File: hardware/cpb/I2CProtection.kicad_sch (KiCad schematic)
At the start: 16 parts, among them Q12 MBT2222ADW1T1, Q13 MBT2222ADW1T1, Q14 BSS138PS,115, Q15 BSS138PS,115

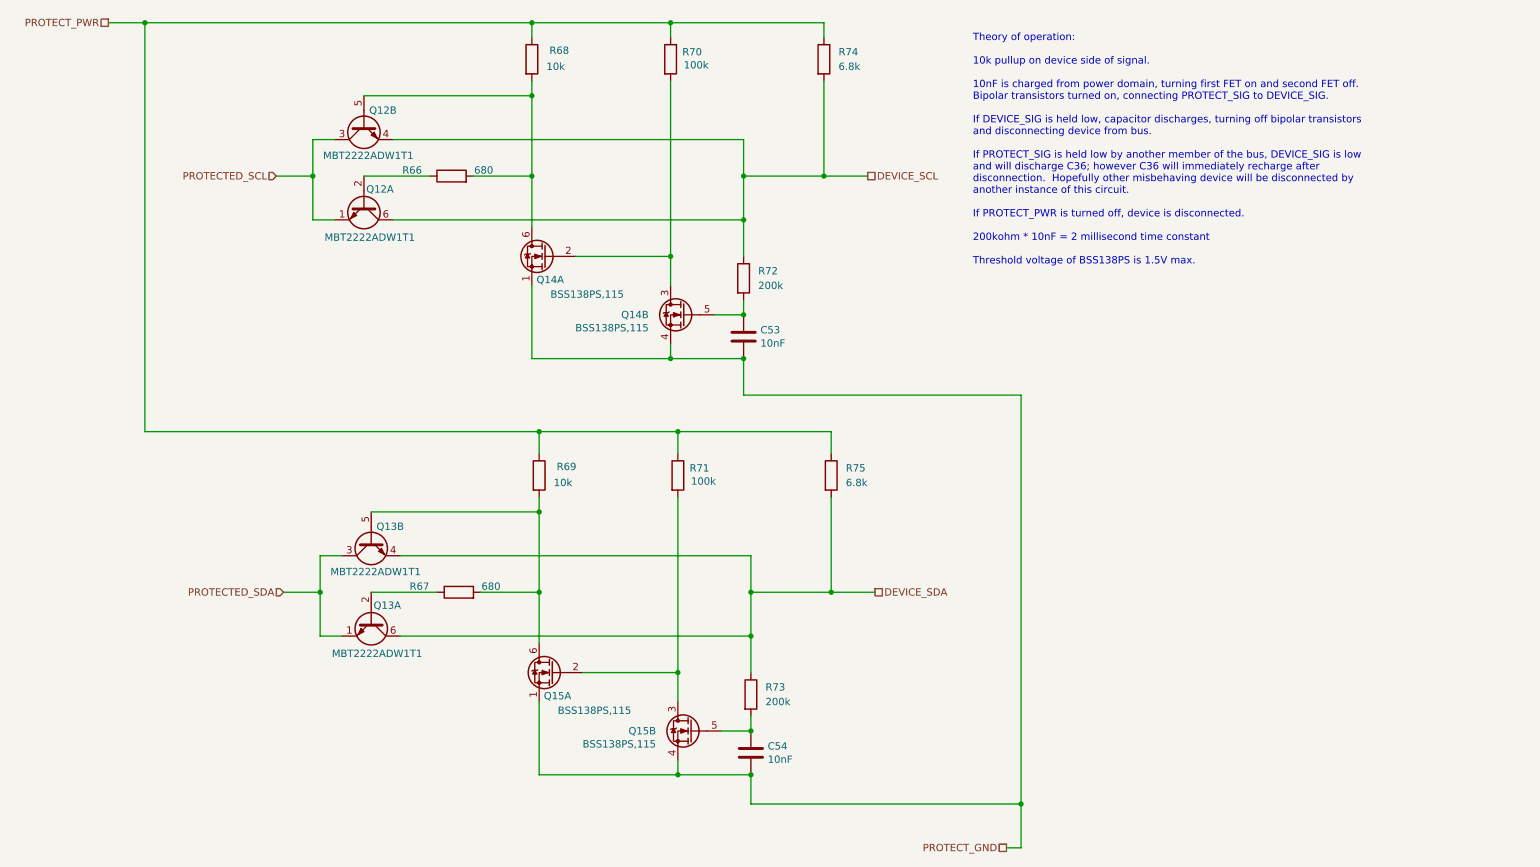
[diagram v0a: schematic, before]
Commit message: hardware/cpb: Transistors on right sorted and bypass capacitors added Moved the transistors into groups then placed next to connectors and placed bypass capacitors near power pins.
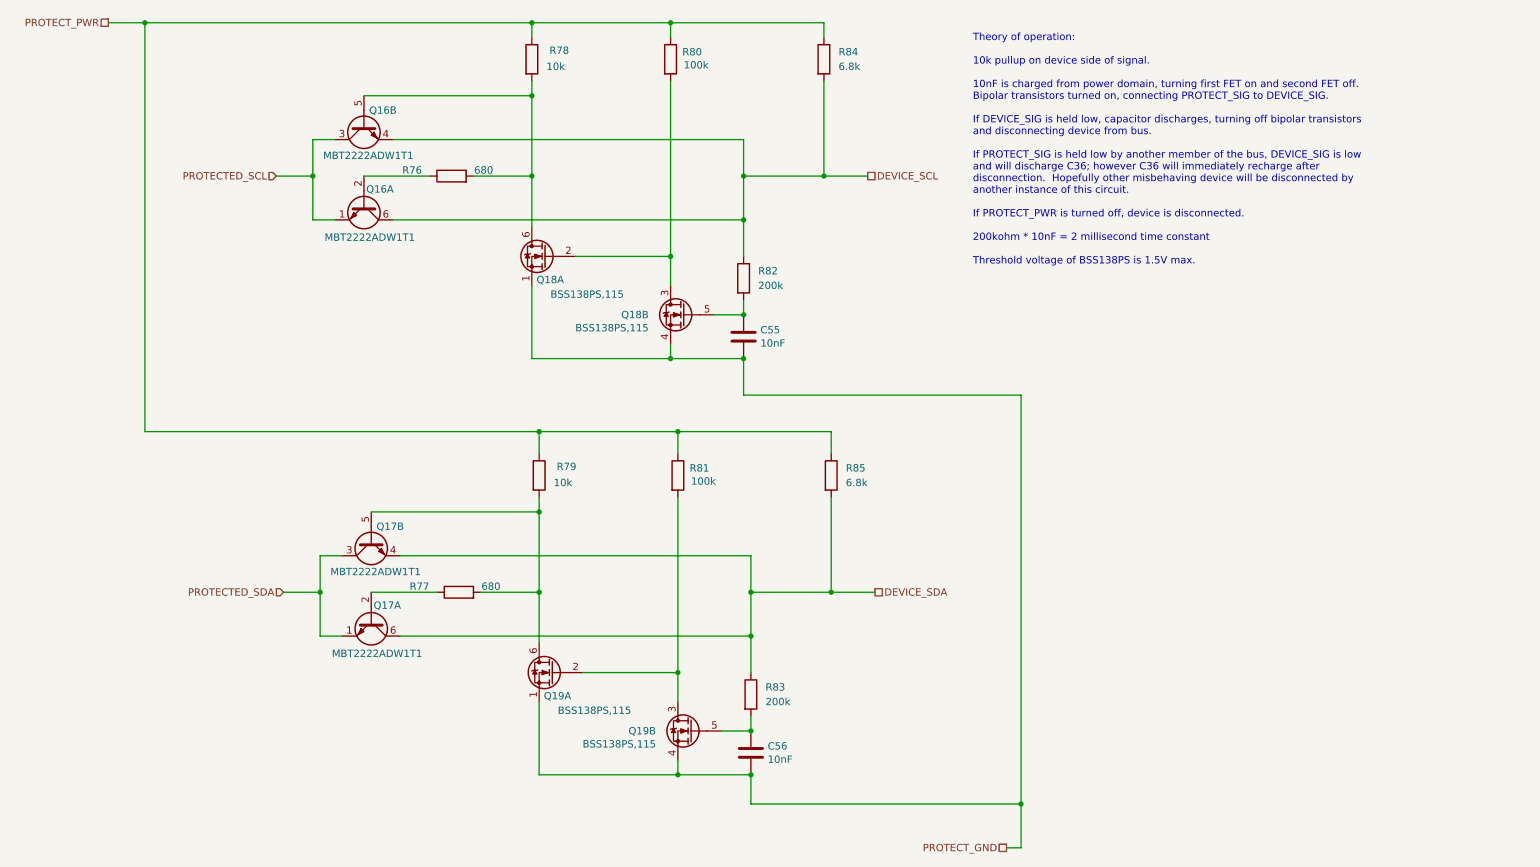
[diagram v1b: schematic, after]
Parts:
- renumbered C53 to C55, C54 to C56, Q12 to Q16, Q13 to Q17, Q14 to Q18, Q15 to Q19, R66 to R76, R67 to R77, R68 to R78, R69 to R79, R70 to R80, R71 to R81, R72 to R82, R73 to R83, R74 to R84, R75 to R85

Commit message: cpb: Bill of materials updates
One layout change will result: some 1206 resistors became 2012.
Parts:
- C55, C56: LCSC (none) -> C100042
- R76, R77: LCSC (none) -> C3996690
- R78, R79: LCSC (none) -> C844918
- R80, R81: LCSC (none) -> C189597
- R82, R83: LCSC (none) -> C118142
- R84, R85: LCSC (none) -> C844805
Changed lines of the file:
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@@
+			)
+		)
+		(property "LCSC" "C844805"
+			(at 161.29 101.6 0)
+			(effects
+				(font
+					(size 1.27 1.27)
+				)
+				(hide yes)
 			)
 		)
@@
 			)
 		)
+		(property "LCSC" "C844918"
+			(at 109.22 29.21 0)
+			(effects
+				(font
+					(size 1.27 1.27)
+				)
+				(hide yes)
+			)
+		)
 		(pin "1"
 		)
@@
 			)
 		)
-		(property "LCSC" ""
+		(property "LCSC" "C100042"
 			(at 147.32 149.86 0)
 			(effects
@@
 		)
 		(property "Description" "Resistor"
+			(at 133.35 29.21 0)
+			(effects
+				(font
+					(size 1.27 1.27)
+				)
+				(hide yes)
+			)
+		)
+		(property "LCSC" "C189597"
 			(at 133.35 29.21 0)
 			(effects
@@
 			)
 		)
+		(property "LCSC" "C118142"
+			(at 146.05 67.31 0)
+			(effects
+				(font
+					(size 1.27 1.27)
+				)
+				(hide yes)
+			)
+		)
 		(pin "1"
 		)
@@
 			)
 		)
+		(property "LCSC" "C3996690"
+			(at 96.52 121.92 0)
+			(effects
+				(font
+					(size 1.27 1.27)
+				)
+				(hide yes)
+			)
+		)
 		(pin "1"
 		)
@@
 		)
 		(property "Description" "Resistor"
+			(at 134.62 101.6 0)
+			(effects
+				(font
+					(size 1.27 1.27)
+				)
+				(hide yes)
+			)
+		)
+		(property "LCSC" "C189597"
 			(at 134.62 101.6 0)
 			(effects
@@
 			)
 		)
+		(property "LCSC" "C118142"
+			(at 147.32 139.7 0)
+			(effects
+				(font
+					(size 1.27 1.27)
+				)
+				(hide yes)
+			)
+		)
 		(pin "1"
 		)
@@
 			)
 		)
+		(property "LCSC" "C3996690"
+			(at 95.25 49.53 0)
+			(effects
+				(font
+					(size 1.27 1.27)
+				)
+				(hide yes)
+			)
+		)
 		(pin "1"
 		)
@@
 			)
 		)
-		(property "LCSC" ""
+		(property "LCSC" "C100042"
 			(at 146.05 77.47 0)
 			(effects
@@
 			)
 		)
+		(property "LCSC" "C844918"
+			(at 110.49 101.6 0)
+			(effects
+				(font
+					(size 1.27 1.27)
+				)
+				(hide yes)
+			)
+		)
 		(pin "1"
 		)
@@
 			(at 160.02 29.21 0)
 			(effects
+				(font
+					(size 1.27 1.27)
+				)
+				(hide yes)
+			)
+		)
+		(property "LCSC" "C844805"
+			(at 160.02 29.21 0)
+			(effects

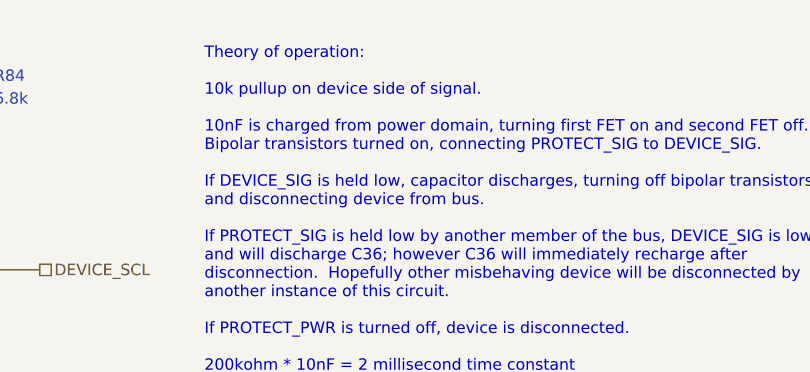
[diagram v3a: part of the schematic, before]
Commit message: cpb: add pours to top and bottom, straighten things
Getting very close, now.
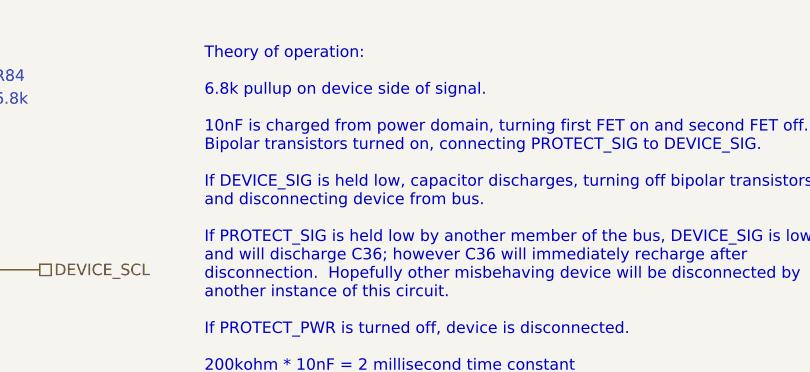
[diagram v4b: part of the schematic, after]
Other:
- note added: "Theory of operation: 6.8k pullup on device side of signal. 10nF is charged from power domain, turning first FET on and second FET off. Bipolar transistors turned on, connecting PROTECT_SIG to DEVICE_SIG. If DEVICE_SIG is held low, capacitor discharges, turning off bipolar transistors and disconnecting device from bus. If PROTECT_SIG is held low by another member of the bus, DEVICE_SIG is low and 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"
- note removed: "Theory of operation: 10k pullup on device side of signal. 10nF is charged from power domain, turning first FET on and second FET off. Bipolar transistors turned on, connecting PROTECT_SIG to DEVICE_SIG. If DEVICE_SIG is held low, capacitor discharges, turning off bipolar transistors and disconnecting device from bus. If PROTECT_SIG is held low by another member of the bus, DEVICE_SIG is low and w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"
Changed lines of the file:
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@@
 		)
 	)
-	(text "Theory of operation:\n\n10k pullup on device side of signal.\n\n10nF is charged from power domain, turning first FET on and second FET off.\nBipolar transistors turned on, connecting PROTECT_SIG to DEVICE_SIG.\n\nIf DEVICE_SIG is held low, capacitor discharges, turning off bipolar transistors\nand disconnecting device from bus.\n\nIf PROTECT_SIG is held low by another member of the bus, DEVICE_SIG is low\nand will discharge C36; however C36 will immediately recharge after\ndisconnection.  Hopefully other misbehaving device will be disconnected by\nanother instance of this circuit.\n\nIf PROTECT_PWR is turned off, device is disconnected.\n\n200kohm * 10nF = 2 millisecond time constant\n\nThreshold voltage of BSS138PS is 1.5V max."
+	(text "Theory of operation:\n\n6.8k pullup on device side of signal.\n\n10nF is charged from power domain, turning first FET on and second FET off.\nBipolar transistors turned on, connecting PROTECT_SIG to DEVICE_SIG.\n\nIf DEVICE_SIG is held low, capacitor discharges, turning off bipolar transistors\nand disconnecting device from bus.\n\nIf PROTECT_SIG is held low by another member of the bus, DEVICE_SIG is low\nand will discharge C36; however C36 will immediately recharge after\ndisconnection.  Hopefully other misbehaving device will be disconnected by\nanother instance of this circuit.\n\nIf PROTECT_PWR is turned off, device is disconnected.\n\n200kohm * 10nF = 2 millisecond time constant\n\nThreshold voltage of BSS138PS is 1.5V max."
 		(exclude_from_sim no)
 		(at 185.928 44.958 0)

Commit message: cpb: update part numbers and attributes
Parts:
- R76, R77: LCSC C3996690 -> C23228
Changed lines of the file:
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@@
 			)
 		)
-		(property "LCSC" "C3996690"
+		(property "LCSC" "C23228"
 			(at 96.52 121.92 0)
 			(effects
@@
 			)
 		)
-		(property "LCSC" "C3996690"
+		(property "LCSC" "C23228"
 			(at 95.25 49.53 0)
 			(effects

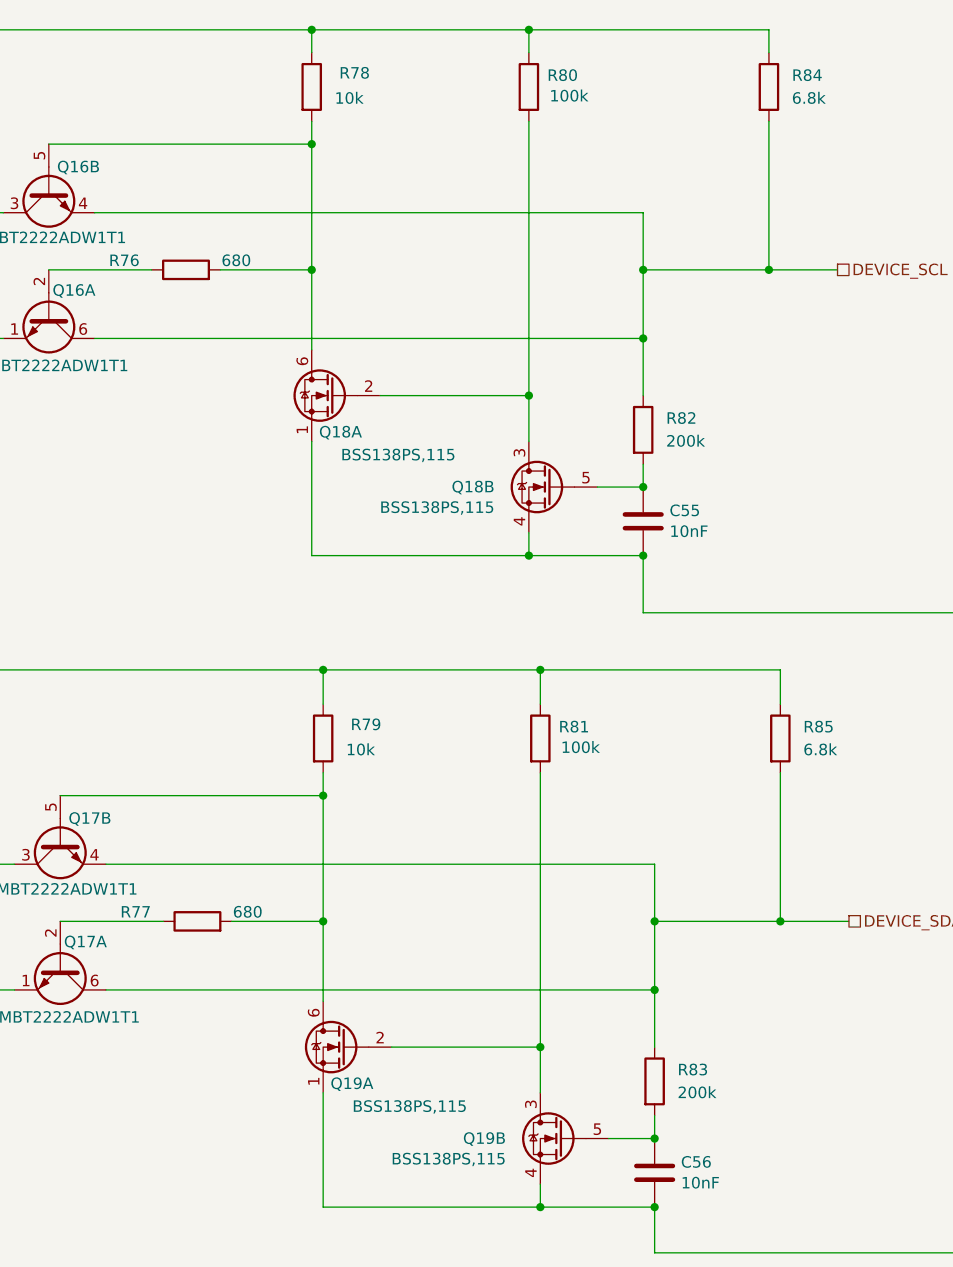
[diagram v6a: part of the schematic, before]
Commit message: hardware/cpb: changed from european to american symbols.
RN parts still are european for now. Changed via TextEdit replace all tool. Device:R --> Device:R_US
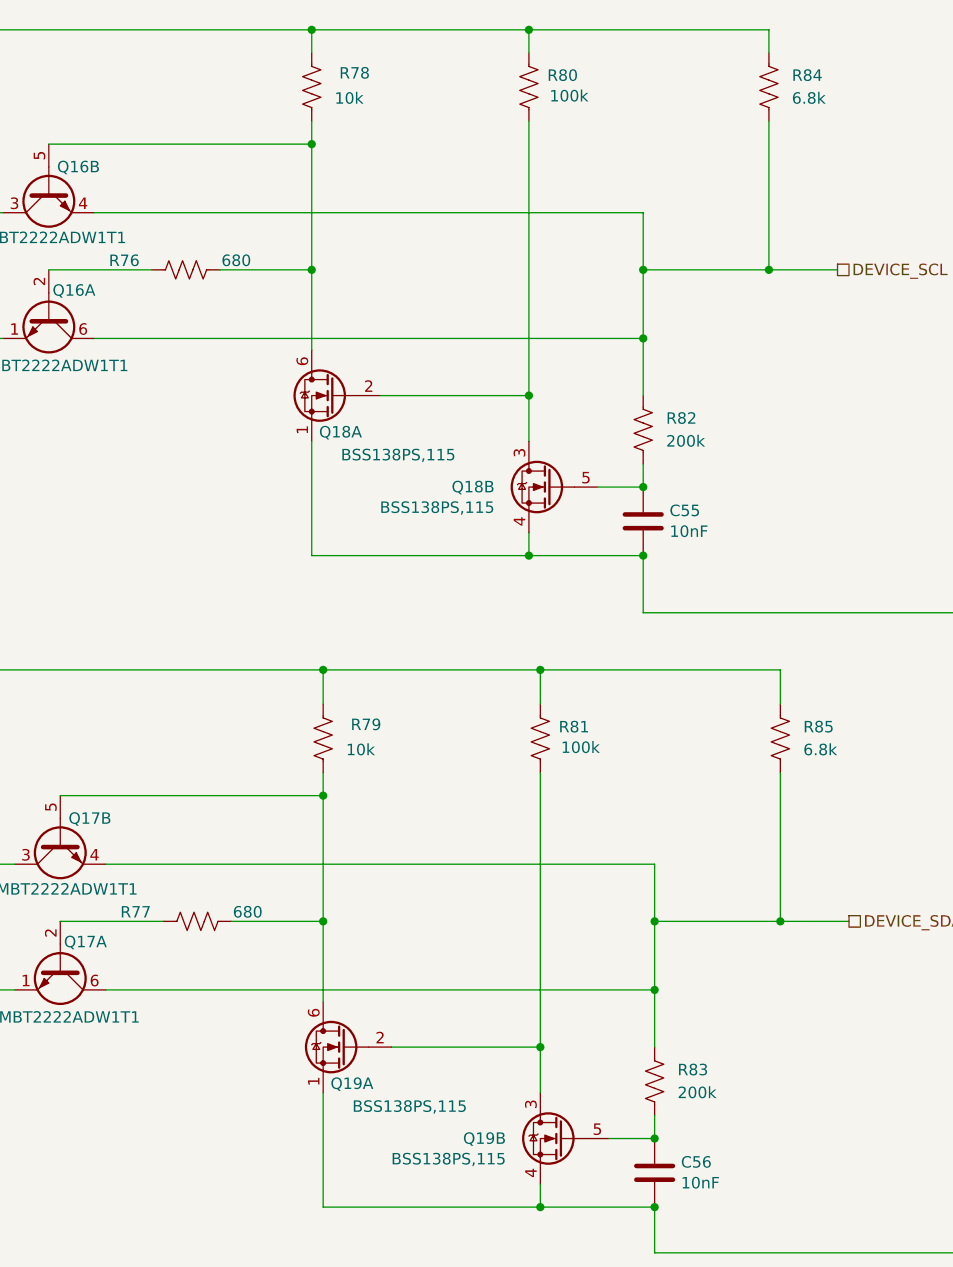
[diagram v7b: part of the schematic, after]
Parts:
- R76, R77, R78, R79, R80, R81, R82, R83, R84, R85: symbol Device:R -> Device:R_US
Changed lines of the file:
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@@
 	)
 	(symbol
-		(lib_id "Device:R")
+		(lib_id "Device:R_US")
 		(at 161.29 101.6 0)
 		(unit 1)
@@
 	)
 	(symbol
-		(lib_id "Device:R")
+		(lib_id "Device:R_US")
 		(at 109.22 29.21 0)
 		(unit 1)
@@
 	)
 	(symbol
-		(lib_id "Device:R")
+		(lib_id "Device:R_US")
 		(at 133.35 29.21 0)
 		(unit 1)
@@
 	)
 	(symbol
-		(lib_id "Device:R")
+		(lib_id "Device:R_US")
 		(at 146.05 67.31 0)
 		(unit 1)
@@
 	)
 	(symbol
-		(lib_id "Device:R")
+		(lib_id "Device:R_US")
 		(at 96.52 121.92 90)
 		(unit 1)
@@
 	)
 	(symbol
-		(lib_id "Device:R")
+		(lib_id "Device:R_US")
 		(at 134.62 101.6 0)
 		(unit 1)
@@
 	)
 	(symbol
-		(lib_id "Device:R")
+		(lib_id "Device:R_US")
 		(at 147.32 139.7 0)
 		(unit 1)
@@
 	)
 	(symbol
-		(lib_id "Device:R")
+		(lib_id "Device:R_US")
 		(at 95.25 49.53 90)
 		(unit 1)
@@
 	)
 	(symbol
-		(lib_id "Device:R")
+		(lib_id "Device:R_US")
 		(at 110.49 101.6 0)
 		(unit 1)
@@
 	)
 	(symbol
-		(lib_id "Device:R")
+		(lib_id "Device:R_US")
 		(at 160.02 29.21 0)
 		(unit 1)
